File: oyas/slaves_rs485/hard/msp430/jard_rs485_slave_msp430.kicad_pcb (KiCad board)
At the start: 2 copper layers, 79.2 x 30 mm, 59 parts, among them J1 EV1, J2 Niveaux, J3 POWER, J4 Débit, J5 Prog MSP, Q1 BPC_FMMT38C, Q2 P03P4L-04, U1 BPC_Alim3_3V, U2 MSP430F1232IDW, U3 MAX485E, Y1 8MHz

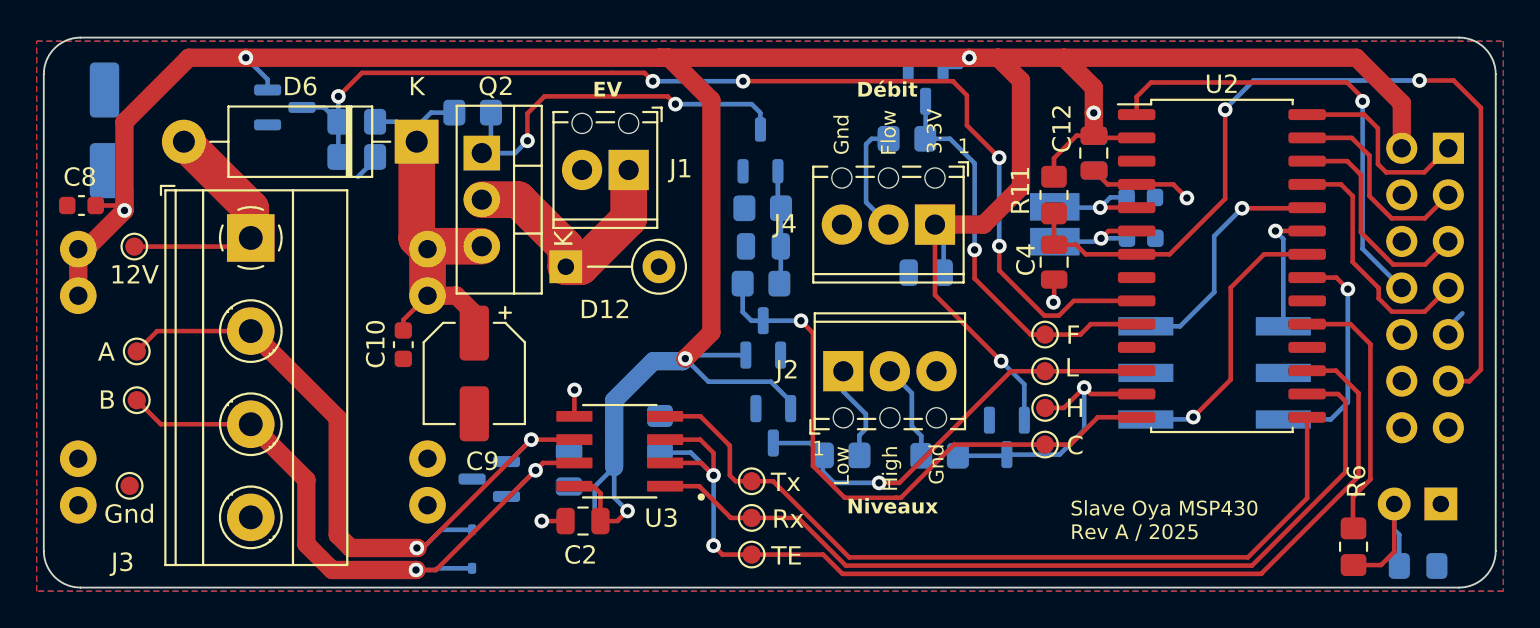
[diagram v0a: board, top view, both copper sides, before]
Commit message: Corrections sur la carte Rev A MSP430
- Pas de pullup interne ds MSP430
- Correction sérigraphie et empreinte connecteur de PROG
- Décalage LED
- Suppression de l'entrée débit
- Empreinte des doides TVS et des capas pour être soudables à la main
- Empreinte D12 horizontale
- C8 et C10 en 805 au lieu de 603
- Grossissement de la sérigraphie de version
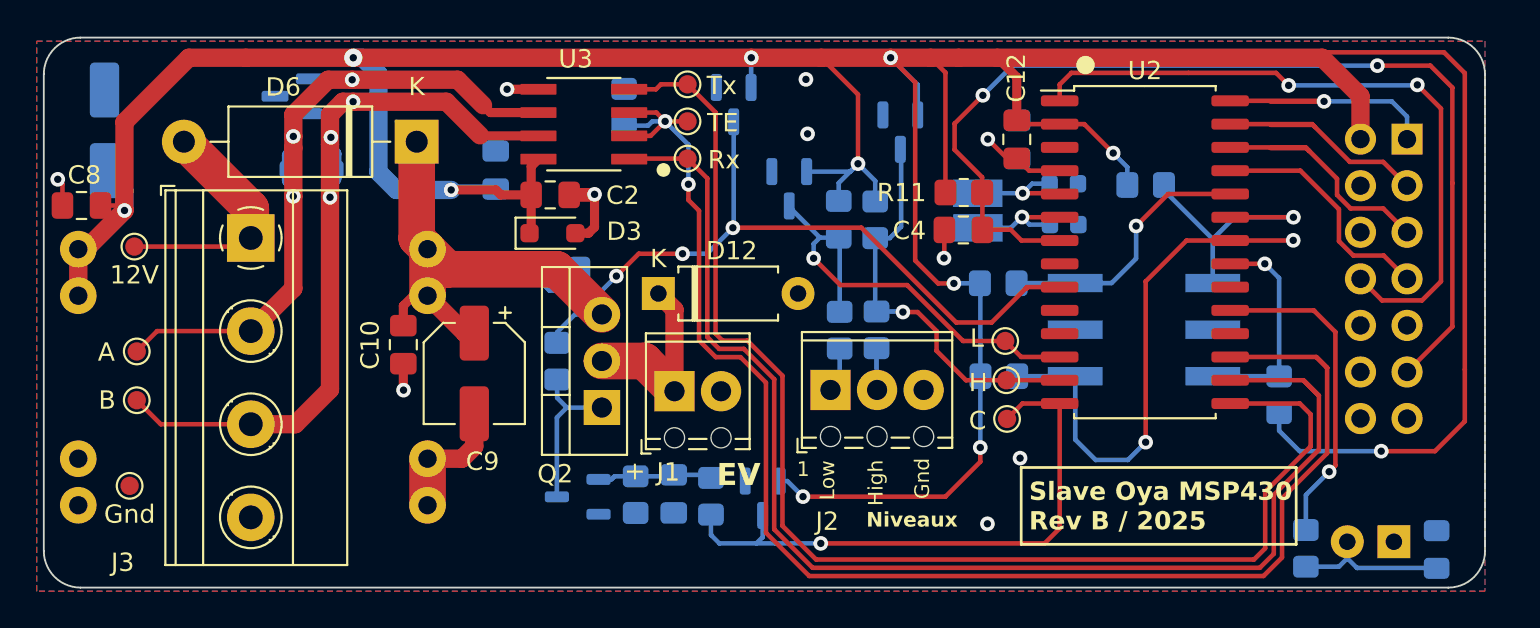
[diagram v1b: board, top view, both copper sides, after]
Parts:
- removed C13: 100nF, Capacitor_SMD:C_0805_2012Metric
- removed D10: BAV99, Package_TO_SOT_SMD:SOT-23
- removed J4: Débit, TerminalBlock_Phoenix:TerminalBlock_Phoenix_MPT-0,5-3-2.54_1x03_P2.54mm_Horizontal
- removed R7: 100, Resistor_SMD:R_0805_2012Metric_Pad1.20x1.40mm_HandSolder
- removed TP10: F, TestPoint:TestPoint_Pad_D1.0mm
- added R12: 100k, Resistor_SMD:R_0805_2012Metric_Pad1.20x1.40mm_HandSolder, B.Cu at (165.5, 105.3)
- added R13: 100k, Resistor_SMD:R_0805_2012Metric_Pad1.20x1.40mm_HandSolder, B.Cu at (173.5, 94.8)
- added R14: 100k, Resistor_SMD:R_0805_2012Metric_Pad1.20x1.40mm_HandSolder, B.Cu at (165.4, 100.2)
- added R15: 100k, Resistor_SMD:R_0805_2012Metric_Pad1.20x1.40mm_HandSolder, B.Cu at (180.8, 106.3)
- added R16: 100k, Resistor_SMD:R_0805_2012Metric_Pad1.20x1.40mm_HandSolder, B.Cu at (158.7, 96.7)
- added R17: 100k, Resistor_SMD:R_0805_2012Metric_Pad1.20x1.40mm_HandSolder, B.Cu at (156.8, 96.7)
- C1, C11, C12, C2, C3, C4: footprint Capacitor_SMD:C_0805_2012Metric -> Capacitor_SMD:C_0805_2012Metric_Pad1.18x1.45mm_HandSolder
- C10, C8: footprint Capacitor_SMD:C_0603_1608Metric -> Capacitor_SMD:C_0805_2012Metric_Pad1.18x1.45mm_HandSolder
- C5, C6: value 15pF -> 10pF
- D12: footprint Diode_THT:D_A-405_P5.08mm_Vertical_KathodeUp -> Diode_THT:D_A-405_P7.62mm_Horizontal
- D3: footprint Diode_SMD:D_SOD-323 -> Diode_SMD:D_SOD-323_HandSoldering; moved to F.Cu
- D5: footprint Diode_SMD:D_SOD-323 -> Diode_SMD:D_SOD-323_HandSoldering
- R6: moved to B.Cu
- moved D7 24.5 mm to (151.0, 90.5), turned to -90 degrees
- moved TP5 23.9 mm to (148.5, 91.4)
- moved D4 23.5 mm to (126.9, 90.0)
- moved D5 22.5 mm to (128.0, 94.0), turned to 0 degrees
- moved TP4 21.9 mm to (148.5, 89.3)
- moved Q1 21.4 mm to (142.5, 111.8), turned to 180 degrees
- moved TP3 19.9 mm to (148.5, 93.4)
- moved R3 17.9 mm to (145.0, 90.6)
- moved U3 17.9 mm to (142.8, 91.5)
- moved C2 17.9 mm to (141.0, 95.4), turned to 180 degrees
- moved D1 17.6 mm to (160.1, 92.0)
- moved R9 17.1 mm to (145.7, 111.7), turned to -90 degrees
- moved C1 16.8 mm to (138.0, 94.0)
- moved D3 15.7 mm to (141.1, 97.5), turned to 0 degrees
- moved Q2 15.3 mm to (143.8, 107.0), turned to 90 degrees
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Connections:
- U2 pad 10: FLOW -> unconnected-(U2-TA0/A2/P2.2-Pad10)
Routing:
- net +3.3V: track 184.2 -> 226.3 mm, vias 7 -> 11
- net TX: track 44.9 -> 70.6 mm
- net RX: track 47.1 -> 70.6 mm
- net FLOW: track 21.9 -> 0.00 mm, vias 1 -> 0
- net TX_EN: track 60.2 -> 80.7 mm
- net POW_MES: track 60.1 -> 41.2 mm, vias 5 -> 3
- net A1: track 15.5 -> 29.1 mm, vias 1 -> 2
- net TEST: track 25.2 -> 37.5 mm, vias 1 -> 2
- net Net-(Q1-C): track 21.0 -> 8.76 mm, vias 2 -> 0
- net GND: track 12.7 -> 22.4 mm, vias 4 -> 10
- net POWER_12V: track 24.0 -> 33.5 mm
- net BUS_B: track 37.5 -> 45.4 mm, vias 2 -> 3
- net A2: track 7.11 -> 14.8 mm
- net Net-(J5-RST): track 49.0 -> 56.4 mm
- net LVL_HIGH: track 15.4 -> 22.1 mm
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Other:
- board size 79.2 x 30 mm -> 78.6 x 30 mm
- board text added: "+"
- board text added: "0"
- board text added: "Slave Oya MSP430 Rev B / 2025"
- board text removed: "3.3V"
- board text removed: "Débit"
- board text removed: "Flow"
- board text removed: "Slave Oya MSP430 Rev A / 2025"

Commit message: Vérification du nouveau design (Rev B)
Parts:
- moved C11 0.23 mm to (166.4, 92.1)
- moved C10 0.09 mm to (132.9, 103.5)
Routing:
- net GND: track 22.4 -> 33.5 mm, vias 10 -> 16
- net A1: track 29.1 -> 25.6 mm, vias 2 -> 1
- net TDO: track 14.2 -> 11.2 mm
- net TDI: track 13.5 -> 11.2 mm
- net TMS: track 14.3 -> 12.3 mm
- net POWER_12V: track 33.5 -> 32.0 mm
- net +3.3V: track 226.3 -> 227.7 mm, vias 11 -> 12
- net LED: track 17.7 -> 16.9 mm

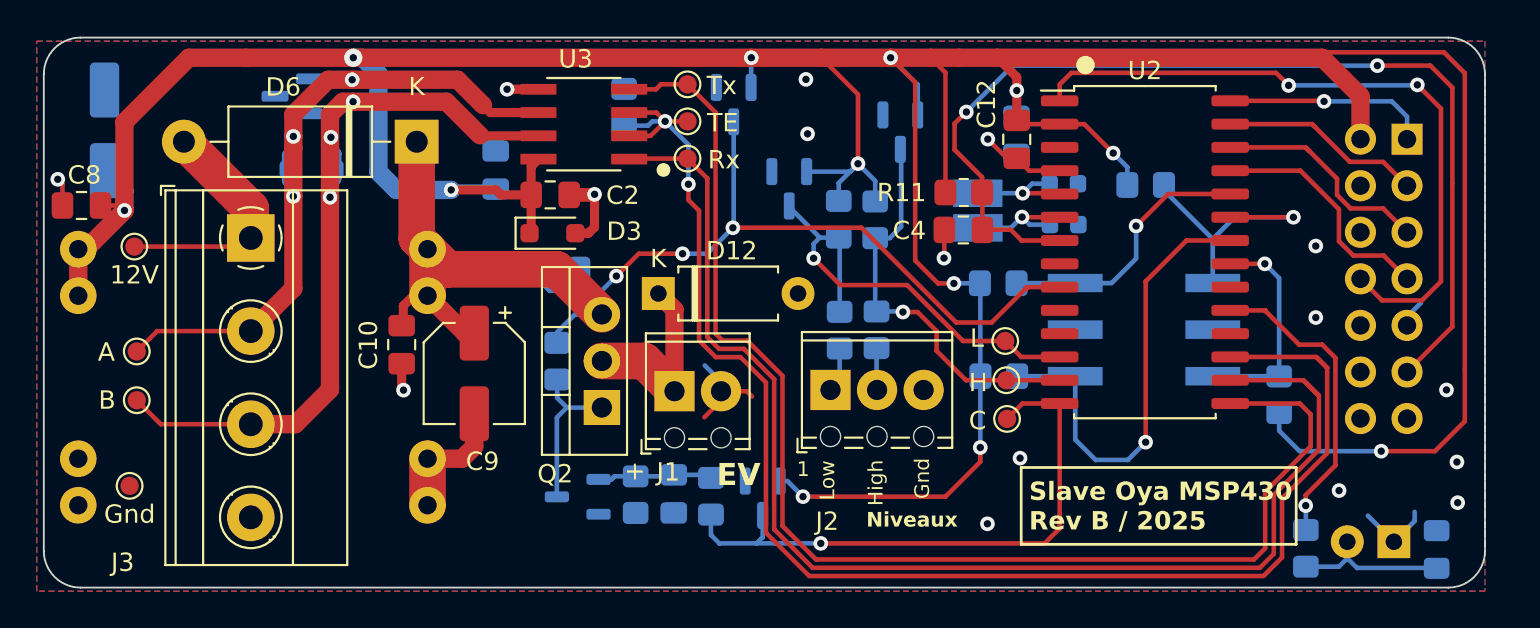
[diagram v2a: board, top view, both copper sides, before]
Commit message: Finitions + Revérification
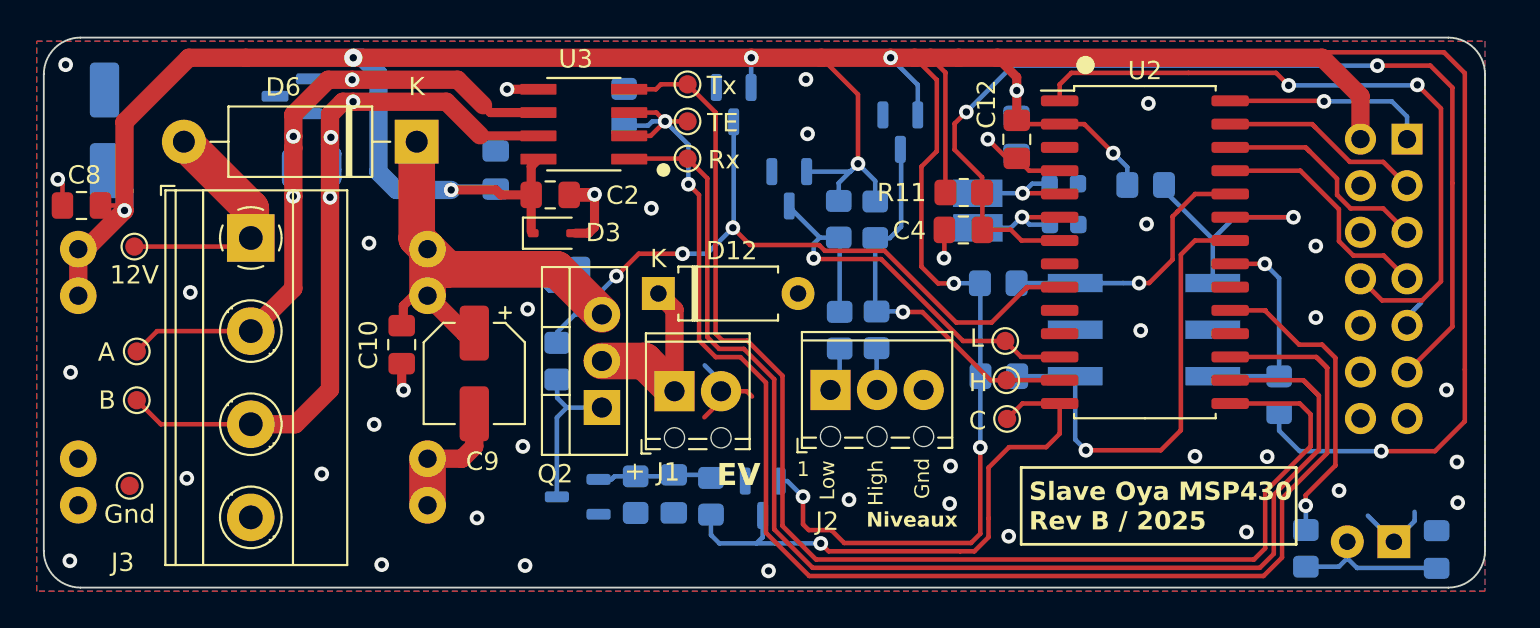
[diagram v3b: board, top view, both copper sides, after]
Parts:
- D3, D5: footprint Diode_SMD:D_SOD-323_HandSoldering -> Diode_SMD:D_SOD-323
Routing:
- net +3.3V: track 227.7 -> 233.0 mm
- net LVL_HIGH: track 22.1 -> 21.5 mm
- net GND: vias 16 -> 39

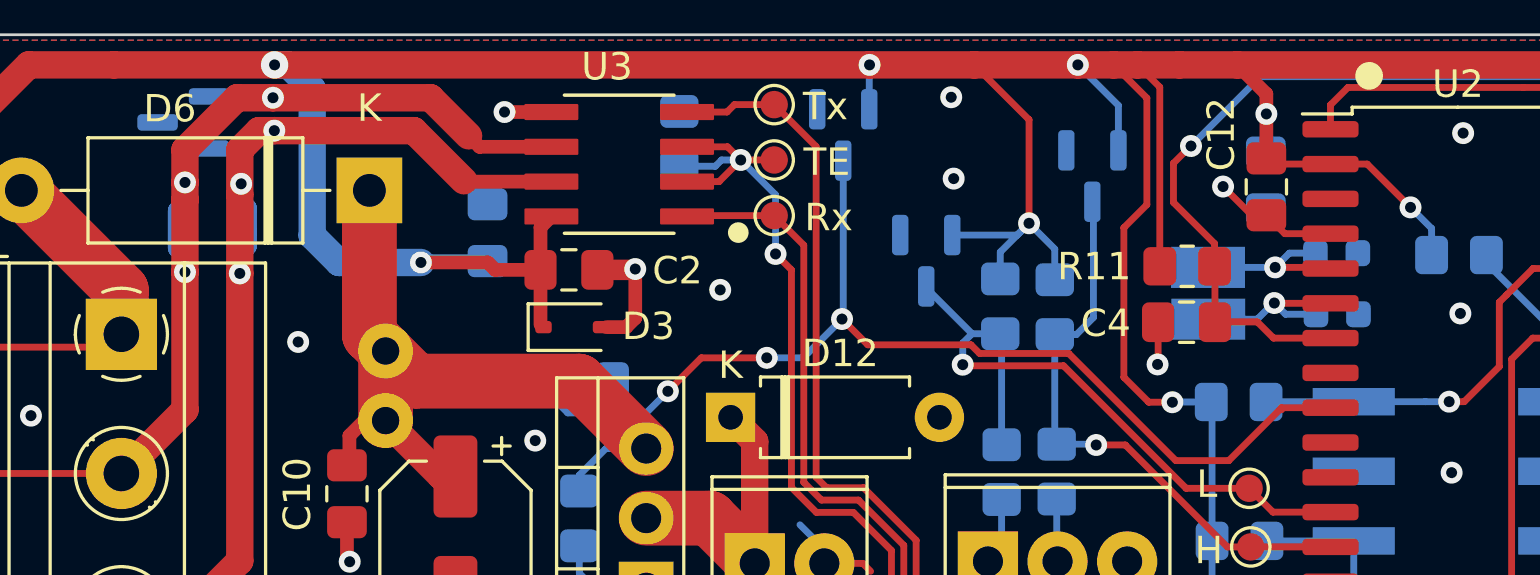
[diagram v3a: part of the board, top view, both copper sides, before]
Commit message: Empreinte TVS
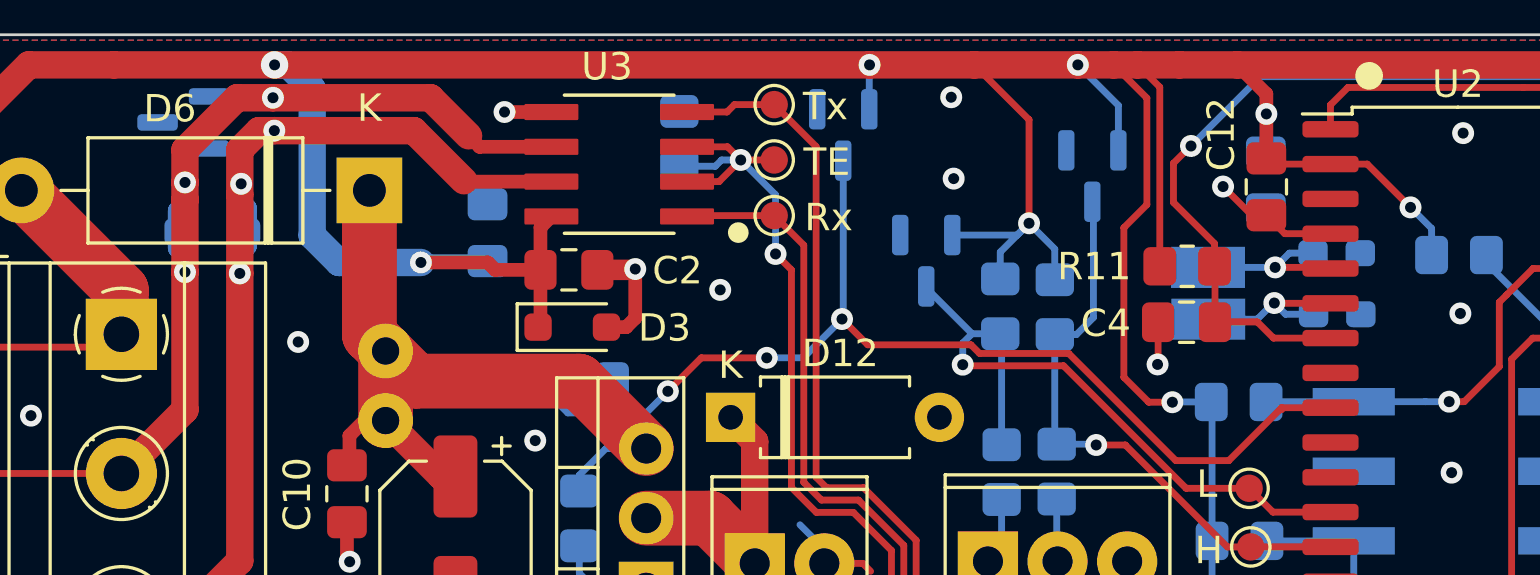
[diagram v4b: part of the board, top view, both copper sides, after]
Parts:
- C5, C6: footprint Capacitor_SMD:C_0603_1608Metric -> Capacitor_SMD:C_0603_1608Metric_Pad1.08x0.95mm_HandSolder
- D3, D5: footprint Diode_SMD:D_SOD-323 -> bpc:BPC_D_SOD-323_HandSoldering
